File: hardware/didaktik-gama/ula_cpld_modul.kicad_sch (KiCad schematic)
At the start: 21 parts, among them J1 do patice ULA (precizní kolík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, J2 RGB + napájení (na J8 hlavní 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, J3 JTAG, U1 XC95144XL-10TQG100C, U2 AMS1117-3.3, X1 14.000 MHz 3,3V

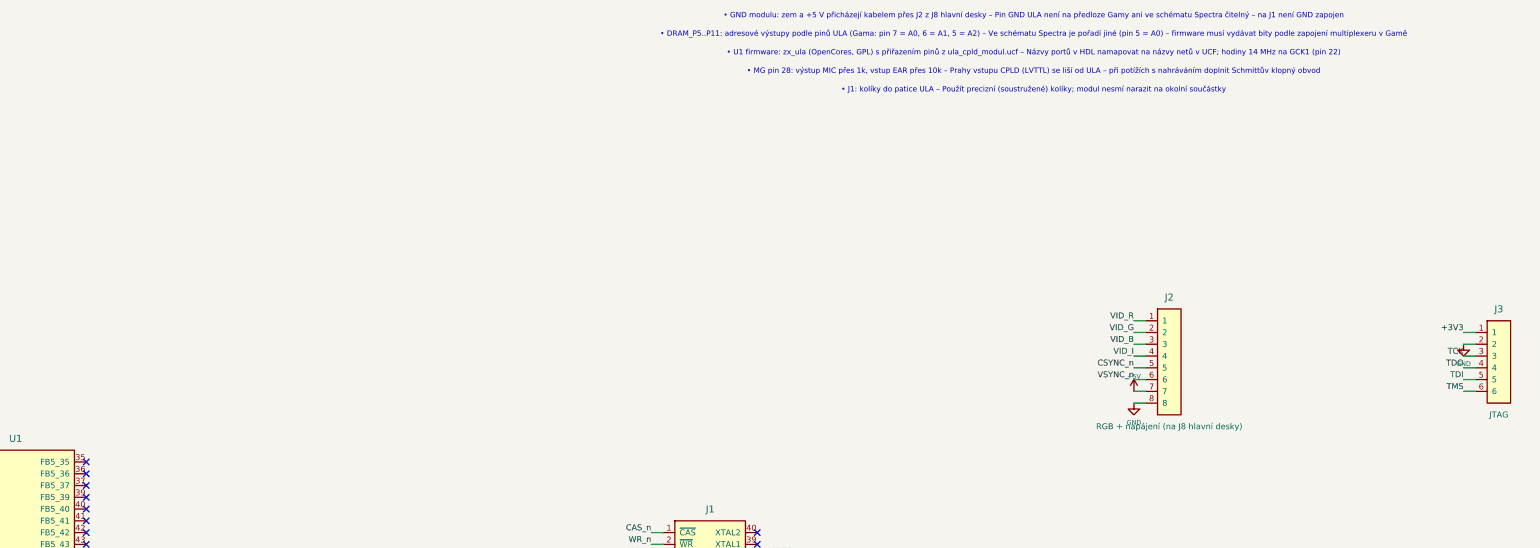
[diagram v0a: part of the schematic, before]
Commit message: Add sound: YM2149/AY on 128K ports, LM386 amplifier and line out
Main board: YM2149F (AY-3-8910 pinout) decoded at FFFD/BFFD via 74HCT11
(A15, A14, A1, IORQ, WR, /M1), 1.75 MHz clock from CPU clock via
74HCT74, resistor mix of AY A/B/C and the beeper, volume pot, LM386 on
VIN to a speaker header and a 3.5 mm line out. Sheet enlarged to A0.
CPLD module: dedicated BEEP output on pin 35, J2/J8 extended to 10 pins.

Co-Authored-By: Claude Opus 5.5 <noreply@anthropic.com>
Claude-Session: https://claude.ai/code/session_01LAVM7Gq9EYiUXiCEdy9ZRx
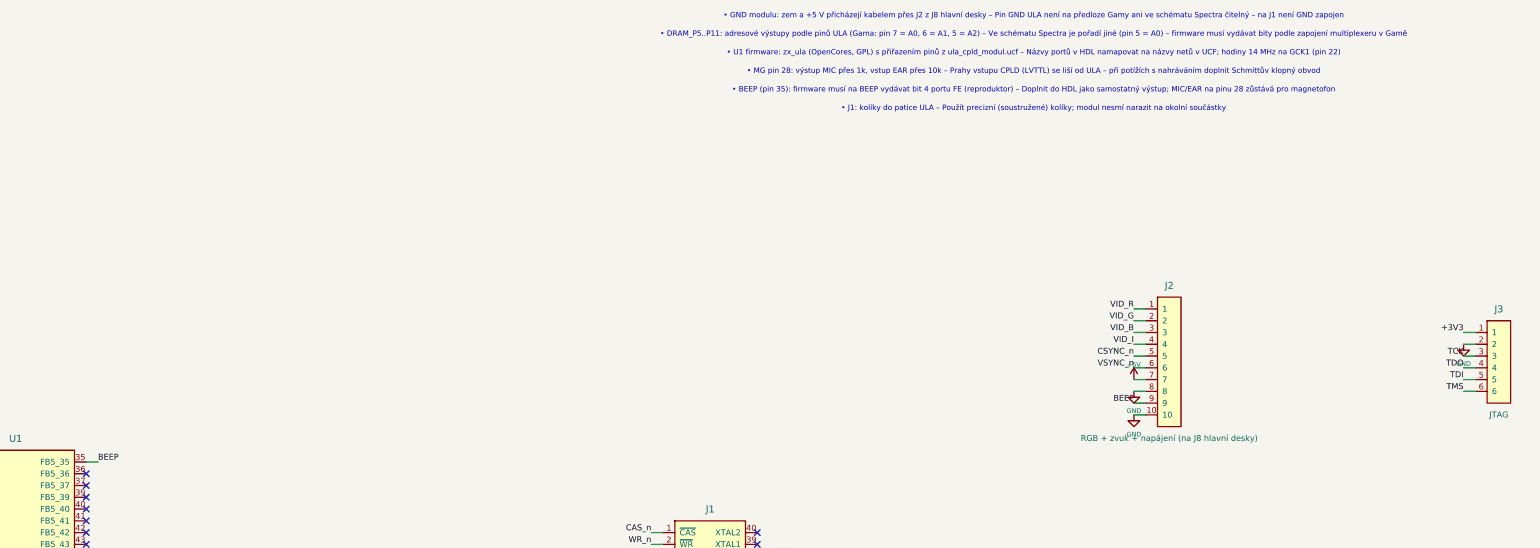
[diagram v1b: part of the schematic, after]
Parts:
- removed C3: 22u, Capacitor_SMD:C_1206_3216Metric, symbol gama:C
- removed J2: RGB + napájení (na J8 hlavní desky), Connector_PinHeader_2.54mm:PinHeader_1x08_P2.54mm_Vertical, symbol gama:CONN_8
- added C10: 100n, Capacitor_SMD:C_0805_2012Metric, symbol gama:C
- added J2: RGB + zvuk + napájení (na J8 hlavní desky), Connector_PinHeader_2.54mm:PinHeader_1x10_P2.54mm_Vertical, symbol gama:CONN_10
- C3: renamed from C4; value 100n -> 22u; footprint Capacitor_SMD:C_0805_2012Metric -> Capacitor_SMD:C_1206_3216Metric
- renumbered C5 to C4, C6 to C5, C7 to C6, C8 to C7, C9 to C8, C10 to C9
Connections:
- net +3V3: now also C10.1
- net +5V: now also J2.7
- net CSYNC_n: now also J2.5
- net GND: now also C10.2, J2.10, J2.8
- net VID_B: now also J2.3
- net VID_G: now also J2.2
- net VID_I: now also J2.4
- net VID_R: now also J2.1
- net VSYNC_n: now also J2.6
- net BEEP: now reaches U1.35 (FB5_35)
- net BEEP: now also J2.9
- no-connect marks 46 -> 45
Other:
- note added: "• BEEP (pin 35): firmware musí na BEEP vydávat bit 4 portu FE (reproduktor) – Doplnit do HDL jako samostatný výstup; MIC/EAR na pinu 28 zůstává pro magnetofon"
- moved on the sheet: C3, C4, C5, C6, C7, C8, C9
